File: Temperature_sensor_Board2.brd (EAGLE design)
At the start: 50.3 x 99.7 mm, 3 parts, among them J1 4_PIN_2MM

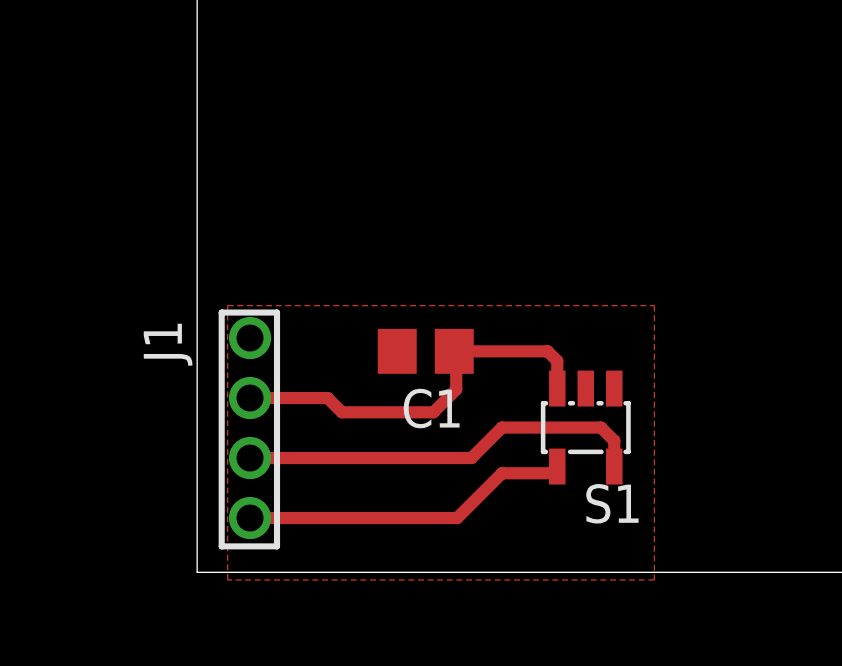
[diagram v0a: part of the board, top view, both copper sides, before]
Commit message: Finished Laser_Array_Temp_Low_BRD_V2.0 and Laser_Array_Temp_High_BRD_V1.0 boards
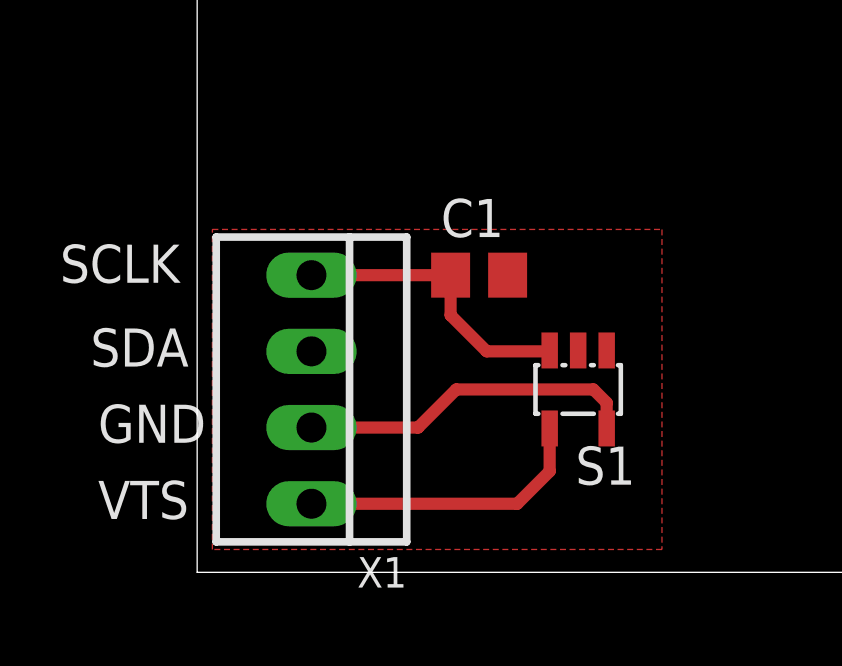
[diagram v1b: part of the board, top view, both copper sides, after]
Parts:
- removed J1: 4_PIN_2MM, Mine:2MM_4PIN
- added X1: 22-23-2041, Mine:22-23-2041
- moved C1 3.10 mm to (8.64, 9.91), turned to 0 degrees
- moved S1 1.30 mm to (11.9, 6.10)
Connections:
- net GND: now also X1.2; no longer J1.2
- net N$2: now also X1.1; no longer J1.4
- net N$3: now also X1.3; no longer J1.6
- net N$4: now also X1.4; no longer J1.8
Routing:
- net N$2: track 13.2 -> 9.79 mm
- net N$3: track 13.6 -> 11.4 mm
- net N$4: track 11.0 -> 9.82 mm
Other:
- board text added: "GND"
- board text added: "SCLK"
- board text added: "SDA"
- board text added: "VTS"
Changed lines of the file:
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@@
 <wire x1="49.51" y1="99.746" x2="-0.762" y2="99.746" width="0" layer="20"/>
 <wire x1="-0.762" y1="99.746" x2="-0.762" y2="0" width="0" layer="20"/>
-<dimension x1="0" y1="0" x2="12.192" y2="-0.508" x3="6.096" y3="-2.286" textsize="1.778" layer="21" dtype="horizontal"/>
+<dimension x1="-0.254" y1="0.762" x2="11.811" y2="13.081" x3="5.7785" y3="-3.048" textsize="1.778" layer="21" dtype="horizontal"/>
+<text x="-4.064" y="4.318" size="1.27" layer="21">GND</text>
+<text x="-4.064" y="1.778" size="1.27" layer="21">VTS</text>
+<text x="-4.318" y="6.858" size="1.27" layer="21">SDA</text>
+<text x="-5.334" y="9.652" size="1.27" layer="21">SCLK</text>
 </plain>
 <attributes>
@@
 </autorouter>
 <elements>
-<element name="C1" library="rcl" package="C0805" value="0.01uF" x="6.858" y="7.366" smashed="yes" rot="R180">
-<attribute name="NAME" x="8.128" y="6.096" size="1.27" layer="25" rot="R180"/>
+<element name="C1" library="rcl" package="C0805" value="0.01uF" x="8.636" y="9.906" smashed="yes">
+<attribute name="NAME" x="7.366" y="11.176" size="1.27" layer="25"/>
 </element>
-<element name="S1" library="Mine" package="SOT23-5L" value="TC74" x="12.192" y="4.826" smashed="yes" rot="R180">
-<attribute name="NAME" x="14.097" y="2.921" size="1.27" layer="25" rot="R180"/>
-<attribute name="VALUE" x="12.827" y="8.255" size="1.27" layer="27" rot="R180"/>
+<element name="S1" library="Mine" package="SOT23-5L" value="TC74" x="11.938" y="6.096" smashed="yes" rot="R180">
+<attribute name="NAME" x="13.843" y="4.191" size="1.27" layer="25" rot="R180"/>
+<attribute name="VALUE" x="8.255" y="6.985" size="1.27" layer="27" rot="R270"/>
 </element>
-<element name="J1" library="Mine" package="2MM_4PIN" value="4_PIN_2MM" x="1.27" y="5.08" smashed="yes" rot="R270">
-<attribute name="NAME" x="-2.54" y="8.43" size="1.27" layer="25" rot="R270"/>
+<element name="X1" library="Mine" package="22-23-2041" value="22-23-2041" x="3.048" y="6.096" smashed="yes" rot="R270">
+<attribute name="MF" value="MOLEX" x="3.048" y="6.096" size="1.778" layer="27" rot="R270" display="off"/>
+<attribute name="OC_FARNELL" value="1462920" x="3.048" y="6.096" size="1.778" layer="27" rot="R270" display="off"/>
+<attribute name="OC_NEWARK" value="38C0355" x="3.048" y="6.096" size="1.778" layer="27" rot="R270" display="off"/>
+<attribute name="MPN" value="22-23-2041" x="3.048" y="6.096" size="1.778" layer="27" rot="R270" display="off"/>
+<attribute name="NAME" x="4.572" y="-0.508" size="1.016" layer="25" ratio="10"/>
 </element>
 </elements>
@@
 <signal name="GND">
 <polygon width="0.3048" layer="1">
-<vertex x="0.254" y="8.89"/>
-<vertex x="14.478" y="8.89"/>
-<vertex x="14.478" y="-0.254"/>
-<vertex x="0.254" y="-0.254"/>
+<vertex x="-0.254" y="11.43"/>
+<vertex x="14.732" y="11.43"/>
+<vertex x="14.732" y="0.762"/>
+<vertex x="-0.254" y="0.762"/>
 </polygon>
-<contactref element="J1" pad="2"/>
+<contactref element="X1" pad="2"/>
 <contactref element="S1" pad="2"/>
 <contactref element="C1" pad="2"/>
 </signal>
 <signal name="N$3">
-<contactref element="J1" pad="6"/>
 <contactref element="S1" pad="5"/>
-<wire x1="13.142" y1="3.526" x2="13.142" y2="4.384" width="0.4064" layer="1"/>
-<wire x1="13.142" y1="4.384" x2="12.7" y2="4.826" width="0.4064" layer="1"/>
-<wire x1="12.7" y1="4.826" x2="9.398" y2="4.826" width="0.4064" layer="1"/>
-<wire x1="9.398" y1="4.826" x2="8.382" y2="3.81" width="0.4064" layer="1"/>
-<wire x1="8.382" y1="3.81" x2="1" y2="3.81" width="0.4064" layer="1"/>
+<contactref element="X1" pad="3"/>
+<wire x1="12.888" y1="4.796" x2="12.888" y2="5.654" width="0.4064" layer="1"/>
+<wire x1="12.888" y1="5.654" x2="12.446" y2="6.096" width="0.4064" layer="1"/>
+<wire x1="12.446" y1="6.096" x2="7.874" y2="6.096" width="0.4064" layer="1"/>
+<wire x1="7.874" y1="6.096" x2="6.604" y2="4.826" width="0.4064" layer="1"/>
+<wire x1="6.604" y1="4.826" x2="3.048" y2="4.826" width="0.4064" layer="1"/>
 </signal>
 <signal name="N$4">
 <contactref element="S1" pad="4"/>
-<contactref element="J1" pad="8"/>
-<wire x1="1" y1="1.81" x2="7.906" y2="1.81" width="0.4064" layer="1"/>
-<wire x1="7.906" y1="1.81" x2="9.398" y2="3.302" width="0.4064" layer="1"/>
-<wire x1="9.398" y1="3.302" x2="11.018" y2="3.302" width="0.4064" layer="1"/>
-<wire x1="11.018" y1="3.302" x2="11.242" y2="3.526" width="0.4064" layer="1"/>
+<contactref element="X1" pad="4"/>
+<wire x1="3.048" y1="2.286" x2="9.906" y2="2.286" width="0.4064" layer="1"/>
+<wire x1="9.906" y1="2.286" x2="10.988" y2="3.368" width="0.4064" layer="1"/>
+<wire x1="10.988" y1="3.368" x2="10.988" y2="4.796" width="0.4064" layer="1"/>
 </signal>
 <signal name="N$2">
-<contactref element="J1" pad="4"/>
 <contactref element="S1" pad="3"/>
 <contactref element="C1" pad="1"/>
-<wire x1="1" y1="5.81" x2="3.588" y2="5.81" width="0.4064" layer="1"/>
-<wire x1="3.588" y1="5.81" x2="4.064" y2="5.334" width="0.4064" layer="1"/>
-<wire x1="4.064" y1="5.334" x2="7.112" y2="5.334" width="0.4064" layer="1"/>
-<wire x1="7.112" y1="5.334" x2="7.874" y2="6.096" width="0.4064" layer="1"/>
-<wire x1="7.874" y1="6.096" x2="7.874" y2="7.3" width="0.4064" layer="1"/>
-<wire x1="7.874" y1="7.3" x2="7.808" y2="7.366" width="0.4064" layer="1"/>
-<wire x1="11.242" y1="6.126" x2="11.242" y2="7.046" width="0.4064" layer="1"/>
-<wire x1="11.242" y1="7.046" x2="10.922" y2="7.366" width="0.4064" layer="1"/>
-<wire x1="10.922" y1="7.366" x2="7.808" y2="7.366" width="0.4064" layer="1"/>
+<wire x1="10.958" y1="7.366" x2="10.988" y2="7.396" width="0.4064" layer="1"/>
+<contactref element="X1" pad="1"/>
+<wire x1="3.048" y1="9.906" x2="7.686" y2="9.906" width="0.4064" layer="1"/>
+<wire x1="10.958" y1="7.366" x2="8.89" y2="7.366" width="0.4064" layer="1"/>
+<wire x1="8.89" y1="7.366" x2="7.686" y2="8.57" width="0.4064" layer="1"/>
+<wire x1="7.686" y1="8.57" x2="7.686" y2="9.906" width="0.4064" layer="1"/>
 </signal>
 </signals>
